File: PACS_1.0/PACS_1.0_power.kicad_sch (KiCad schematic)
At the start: 0 parts

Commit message: Added Bucks, Temp and Light Sensor
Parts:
- added BT1: 7.2V, symbol Device:Battery
- added C10, C11, C7, C8: 10uF, symbol Device:C
- added C12, C13, C4, C9: 0.1uF, symbol Device:C
- added C14, C15, C5, C6: 22uF, symbol Device:C
- added L1: 3.3uH, symbol Device:L
- added L2: 4.7uH, symbol Device:L
- added R1, R3, R4, R6: 10k, symbol Device:R
- added R2: 33.2k, symbol Device:R
- added R5: 54.9k, symbol Device:R
- added U2, U3: TPS562201DDCR, TPS562201DDCR:SOT95P280X110-6N, symbol TPS562201DDCR:TPS562201DDCR
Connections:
- new net: R3.2, U2.5 (EN)
- new net: R5.1, R6.1, U3.4 (VFB)
- new net: C4.1, U2.6 (VBST)
- new net: C4.2, L1.1, U2.2 (SW)
- new net: C13.2, L2.1, U3.2 (SW)
- new net: R4.2, U3.5 (EN)
- new net: C13.1, U3.6 (VBST)
- new net: R1.1, R2.1, U2.4 (VFB)
- new net +3.3V: C5.1, C6.1, L1.2, R2.2
- new net +5V: C14.1, C15.1, L2.2, R5.2
- new net EN3.3V: R3.1
- new net EN5V: R4.1
- new net GND: C10.2, C11.2, C12.2, C14.2, C15.2, C5.2, C6.2, C7.2, C8.2, C9.2, R1.2, R6.2, U2.1 (GND), U3.1 (GND)
- new net VIN: C10.1, C11.1, C12.1, C7.1, C8.1, C9.1, U2.3 (VIN), U3.3 (VIN)

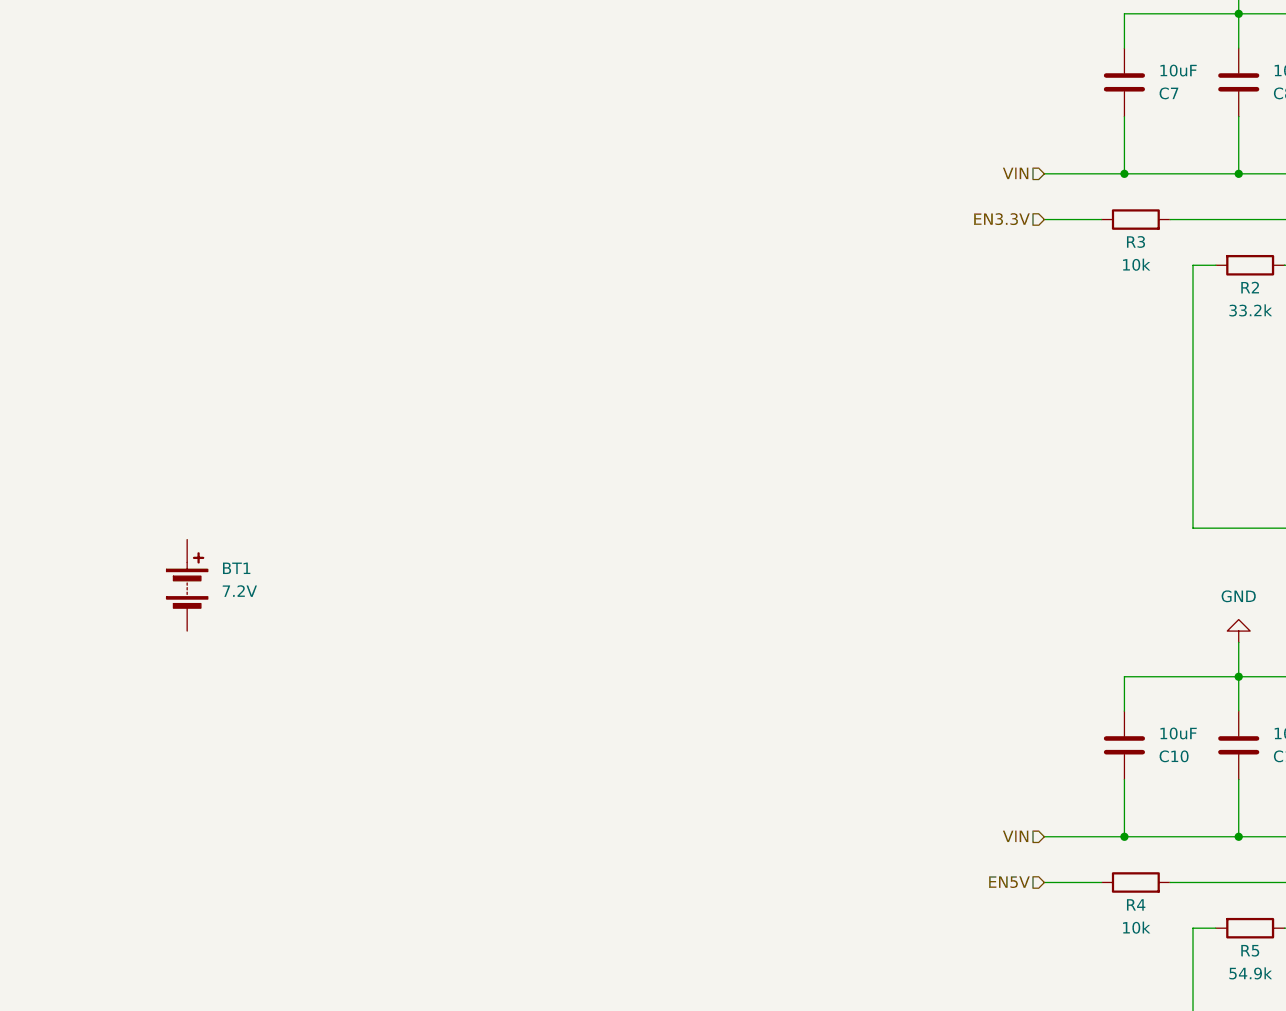
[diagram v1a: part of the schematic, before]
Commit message: New Changes
We had the discussion about water pump, INA, LEDS, and battery solution. Not much changes from previous night.
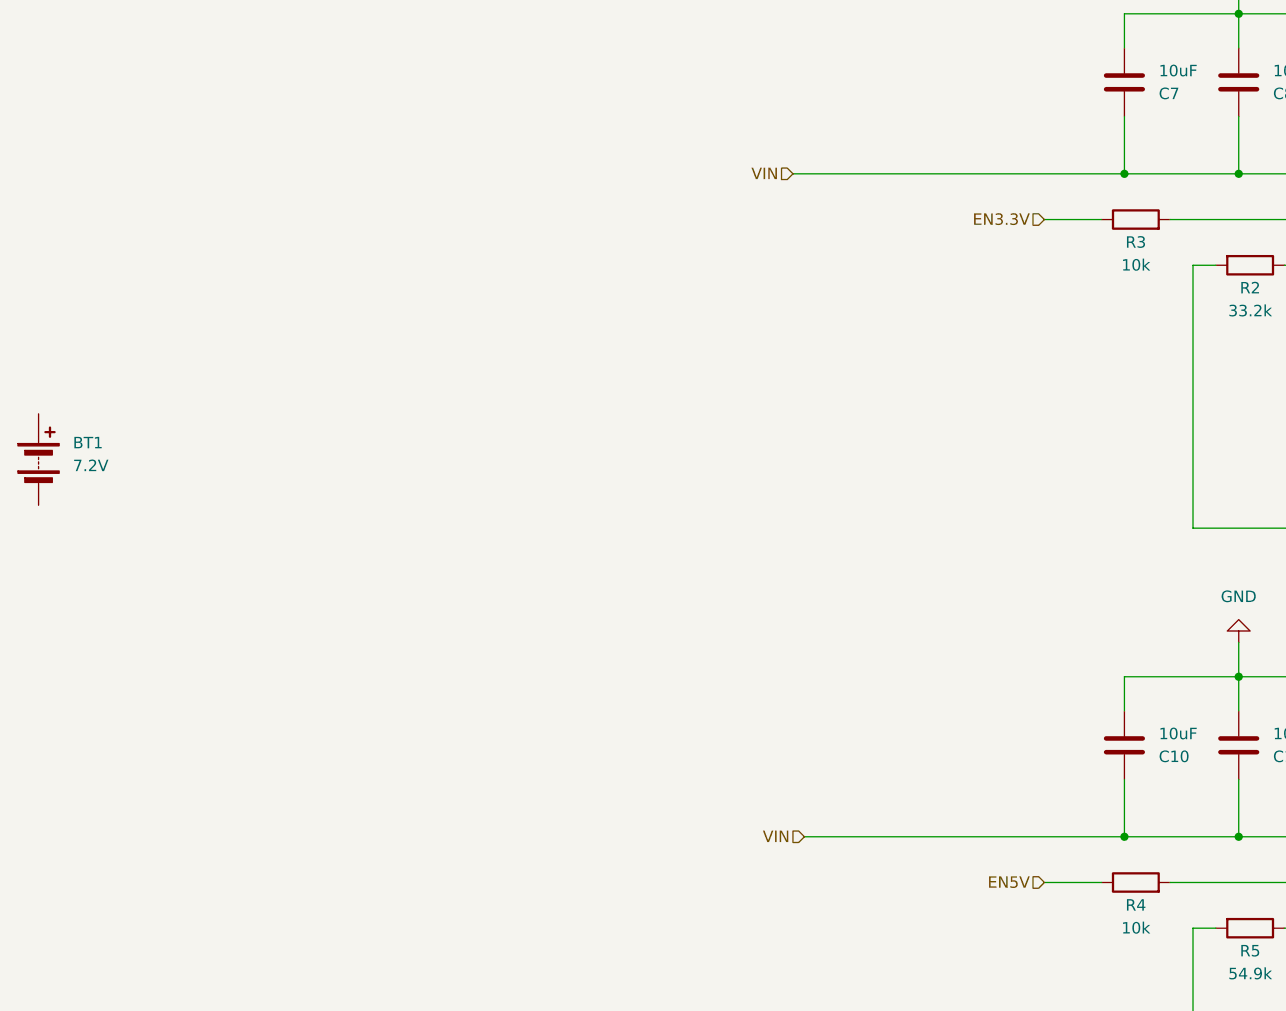
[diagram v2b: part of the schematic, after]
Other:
- moved on the sheet: BT1
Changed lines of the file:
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@@
 	(wire
 		(pts
-			(xy 143.51 118.11) (xy 152.4 118.11)
+			(xy 116.84 118.11) (xy 152.4 118.11)
 		)
 		(stroke
@@
 	(wire
 		(pts
-			(xy 143.51 44.45) (xy 152.4 44.45)
+			(xy 115.57 44.45) (xy 152.4 44.45)
 		)
 		(stroke
@@
 	(hierarchical_label "VIN"
 		(shape input)
-		(at 143.51 44.45 180)
+		(at 115.57 44.45 180)
 		(fields_autoplaced yes)
 		(effects
@@
 	(hierarchical_label "VIN"
 		(shape input)
-		(at 143.51 118.11 180)
+		(at 116.84 118.11 180)
 		(fields_autoplaced yes)
 		(effects
@@
 	(symbol
 		(lib_id "Device:Battery")
-		(at 48.26 90.17 0)
+		(at 31.75 76.2 0)
 		(unit 1)
 		(exclude_from_sim no)
@@
 		(fields_autoplaced yes)
 		(property "Reference" "BT1"
-			(at 52.07 88.3284 0)
+			(at 35.56 74.3584 0)
 			(effects
 				(font
@@
 		)
 		(property "Value" "7.2V"
-			(at 52.07 90.8684 0)
+			(at 35.56 76.8984 0)
 			(effects
 				(font
@@
 		)
 		(property "Footprint" ""
-			(at 48.26 88.646 90)
+			(at 31.75 74.676 90)
 			(effects
 				(font
@@
 		)
 		(property "Datasheet" "~"
-			(at 48.26 88.646 90)
+			(at 31.75 74.676 90)
 			(effects
 				(font
@@
 		)
 		(property "Description" "Multiple-cell battery"
-			(at 48.26 90.17 0)
-			(effects
-				(font
+			(at 31.75 76.2 0)
+			(effects
+				(font

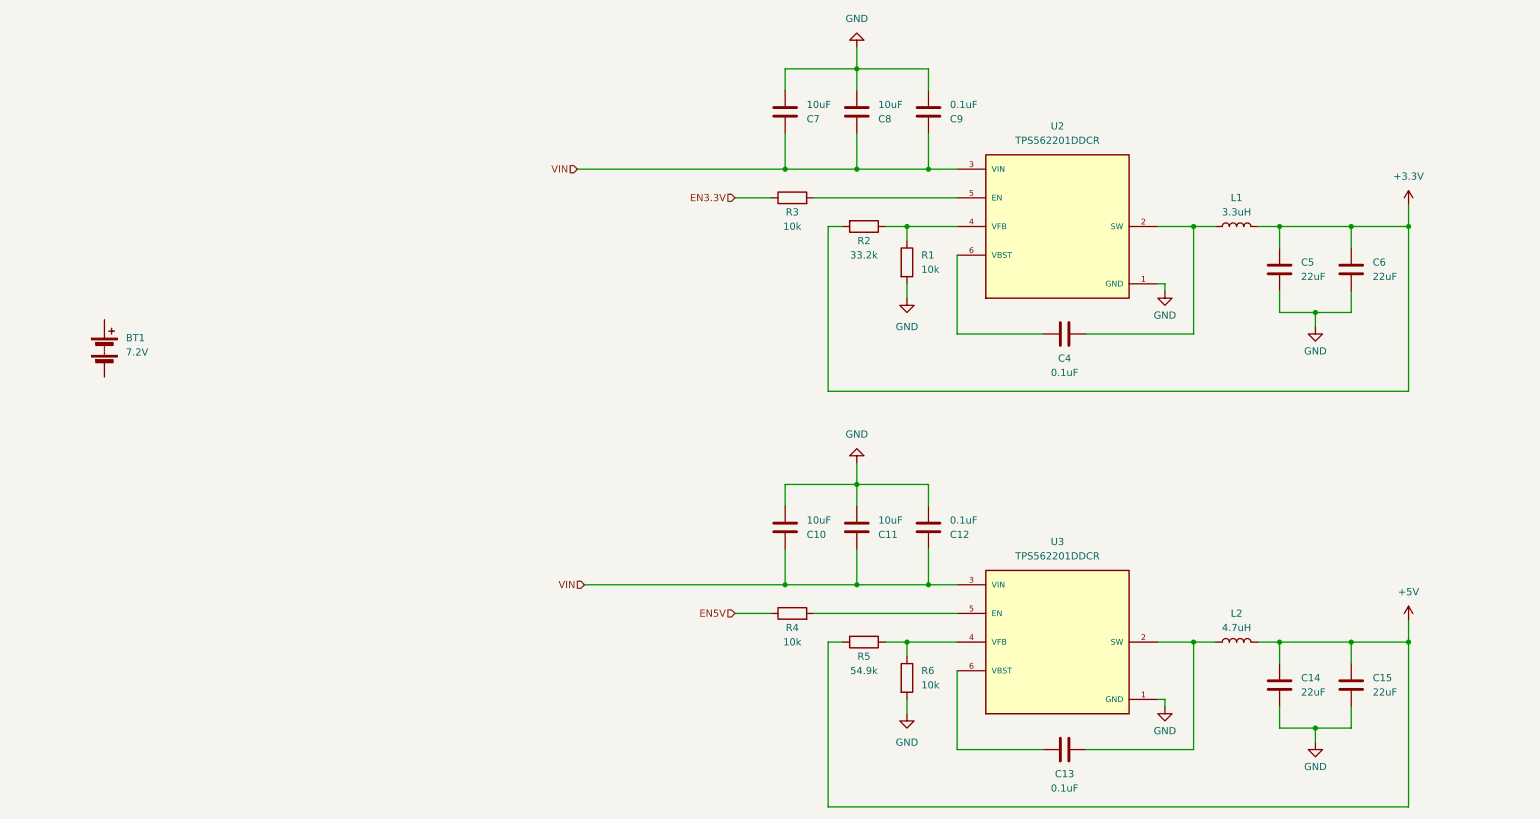
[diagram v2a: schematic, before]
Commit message: Added Water level sensor and start of Pump
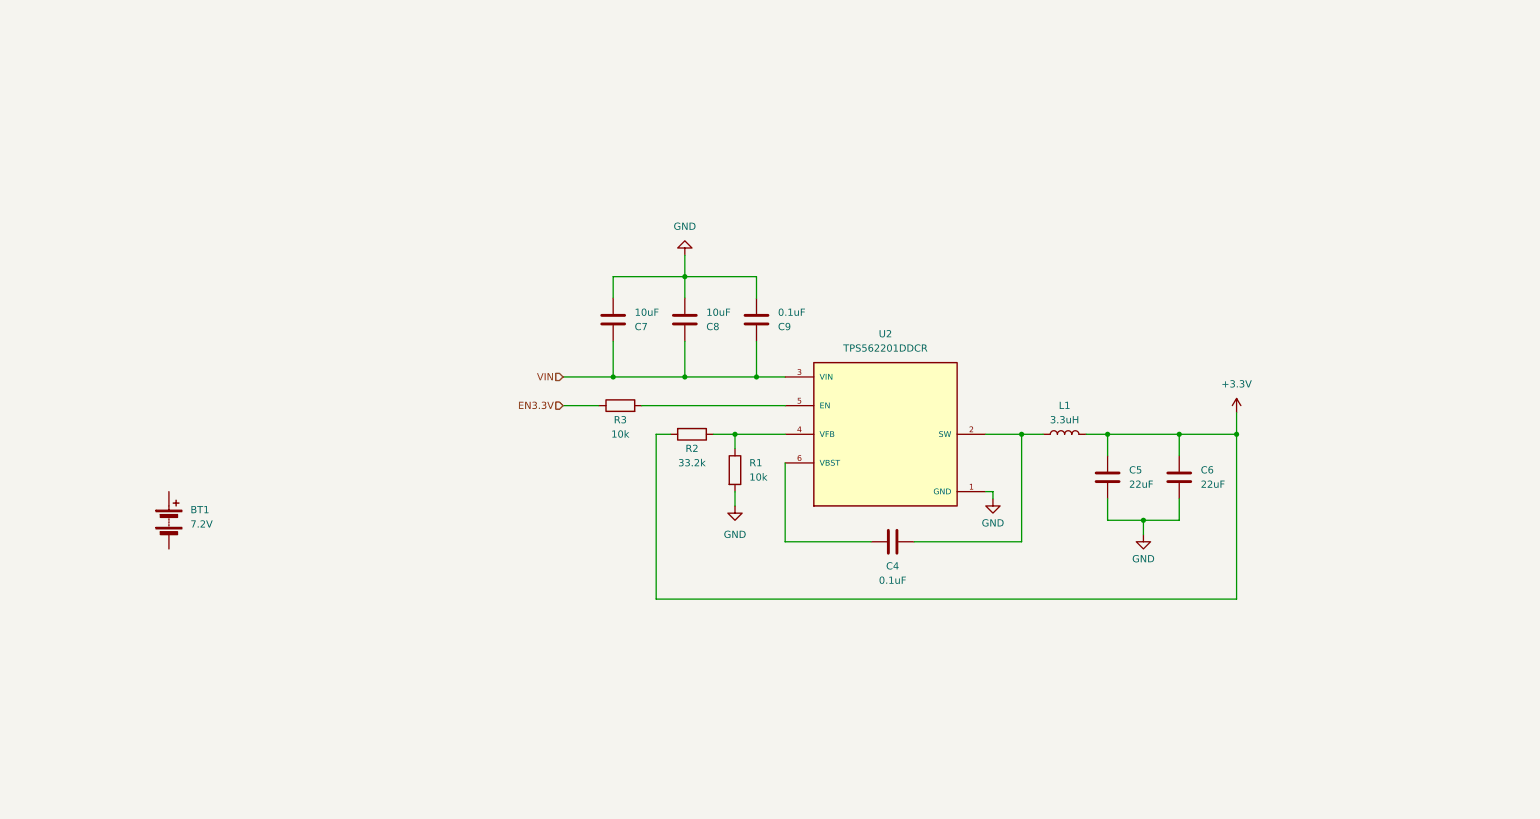
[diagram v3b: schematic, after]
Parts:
- removed C10, C11: 10uF, symbol Device:C
- removed C12, C13: 0.1uF, symbol Device:C
- removed C14, C15: 22uF, symbol Device:C
- removed L2: 4.7uH, symbol Device:L
- removed R4, R6: 10k, symbol Device:R
- removed R5: 54.9k, symbol Device:R
- removed U3: TPS562201DDCR, TPS562201DDCR:SOT95P280X110-6N, symbol TPS562201DDCR:TPS562201DDCR
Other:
- moved on the sheet: BT1, C4, C5, C6, C7, C8, C9, L1, R1, R2, R3, U2

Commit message: Finished Zigbee Module
also fixed some library issues
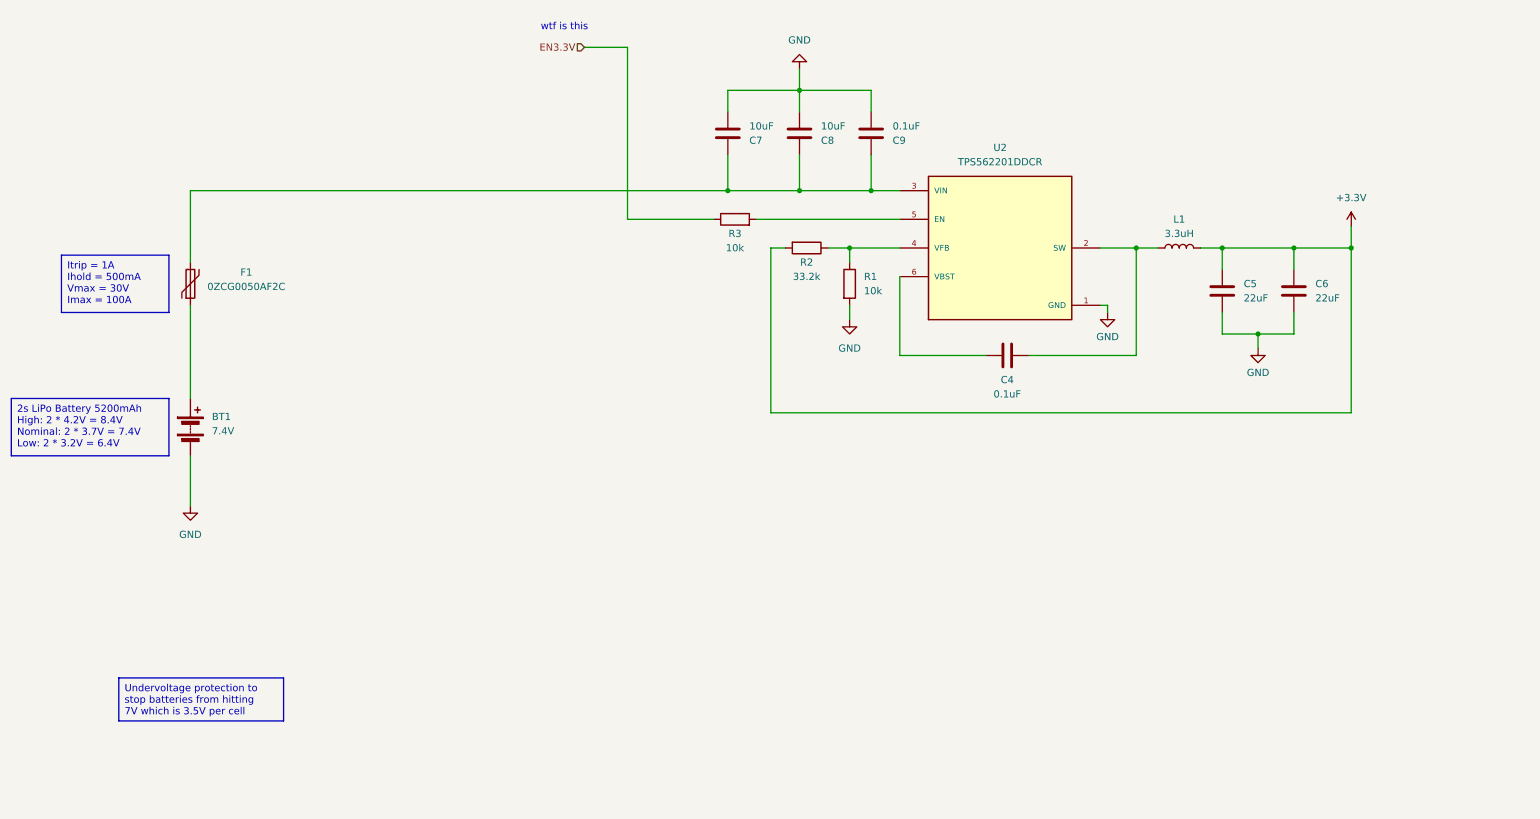
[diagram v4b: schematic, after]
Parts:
- added F1: 0ZCG0050AF2C, symbol Device:Polyfuse
- BT1: value 7.2V -> 7.4V
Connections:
- net GND: now also BT1.2 (-)
- net at BT1.1 (+): now also F1.1
- net VIN: no longer names the net of C7.1, C8.1, C9.1, U2.3 (VIN)
- net VIN: now also F1.2
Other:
- note added: "wtf is this"
- moved on the sheet: BT1, C4, C5, C6, C7, C8, C9, L1, R1, R2, R3, U2

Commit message: Added Undervoltage Protection, removed LED kicad
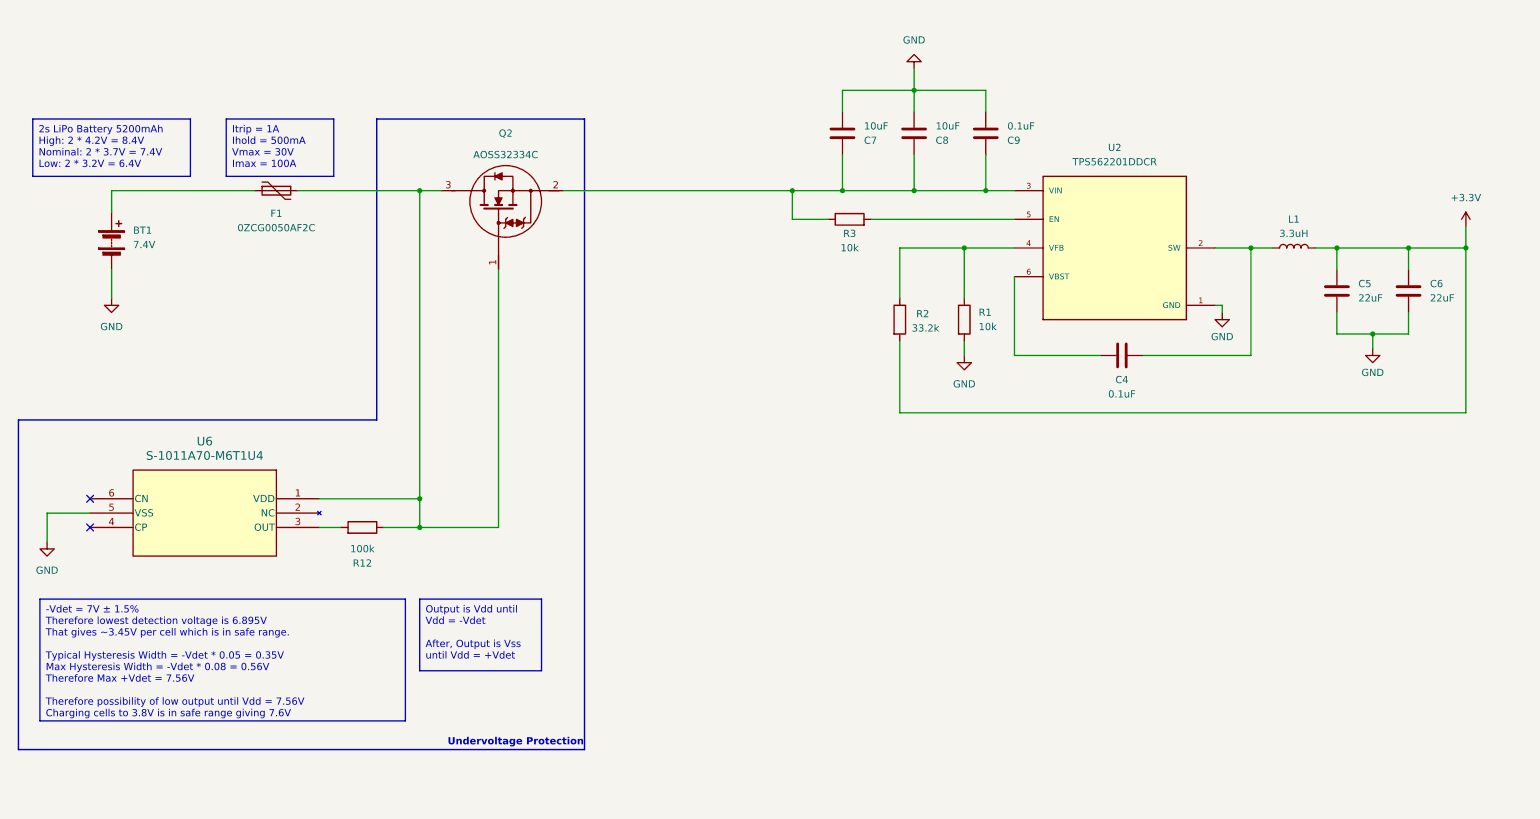
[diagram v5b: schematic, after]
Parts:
- added Q2: ~, Package_TO_SOT_SMD:TSOT-23, symbol AOSS32334C:AOSS32334C
- added R12: 100k, symbol Device:R
- added U6: S-1011A70-M6T1U4, SOT236-A-PKG_MP006-A-P-SD-2.1_ABL, symbol S-1011A70-M6T1U4:S-1011A70-M6T1U4
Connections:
- net EN3.3V is gone; now on an unnamed net: R3.1
- net GND: now also U6.5 (VSS)
- net at C7.1, C8.1, C9.1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: now also Q2.2; no longer F1.2
- new net: F1.2, Q2.1, Q2.3, R12.1, U6.1 (VDD)
- new net: R12.2, U6.3 (OUT)
- no-connect marks 0 -> 2
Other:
- note added: "Undervoltage Protection"
- note removed: "wtf is this"
- moved on the sheet: BT1, C4, C5, C6, C7, C8, C9, F1, L1, R1, R2, R3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

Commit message: Finished 1.0 (NO INA INCLUDED)
Finished PACS 1.0 sheets, Power sheet needs considerations, no INA yet.
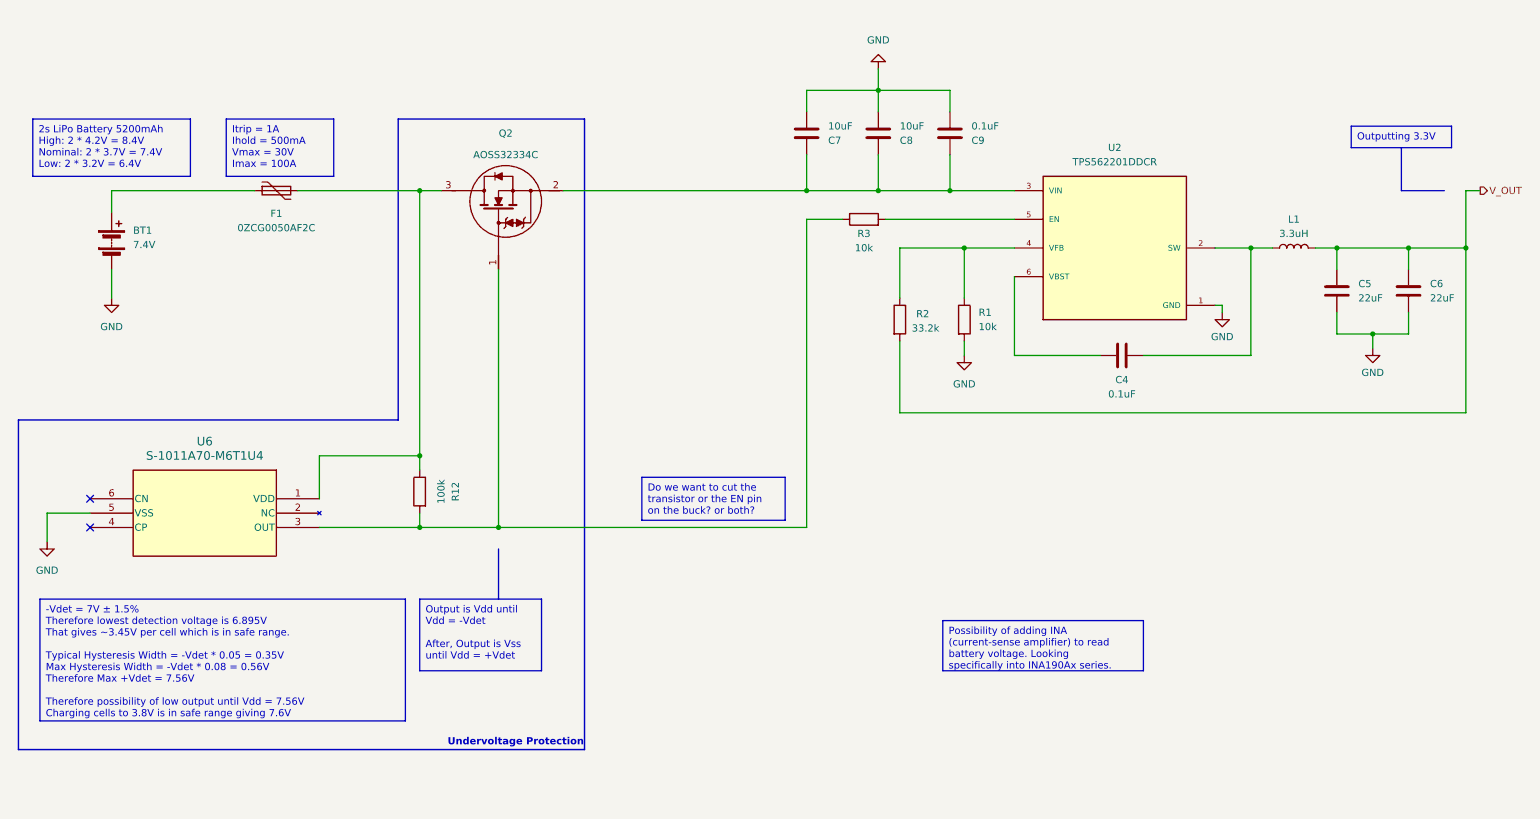
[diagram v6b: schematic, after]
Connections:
- net at C7.1, C8.1, C9.1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: no longer R3.1
- net at F1.2, Q2.3, R12.1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: no longer Q2.1
- net at R12.2, U6.3 (OUT): now also Q2.1, R3.1
- net +3.3V renamed V_OUT
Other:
- title: (none) -> Power
- moved on the sheet: C7, C8, C9, R3
